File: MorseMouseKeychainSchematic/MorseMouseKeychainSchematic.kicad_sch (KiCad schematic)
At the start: 10 parts, among them J1 TP4056 with Protecive Diode, J2 ESP32-C3 SuperMini, J3 HW-504 Joystick Controller, J4 5v Boost Converter, J5 USB_C_Receptacle_USB2.0_16P, SW1 SW_Push

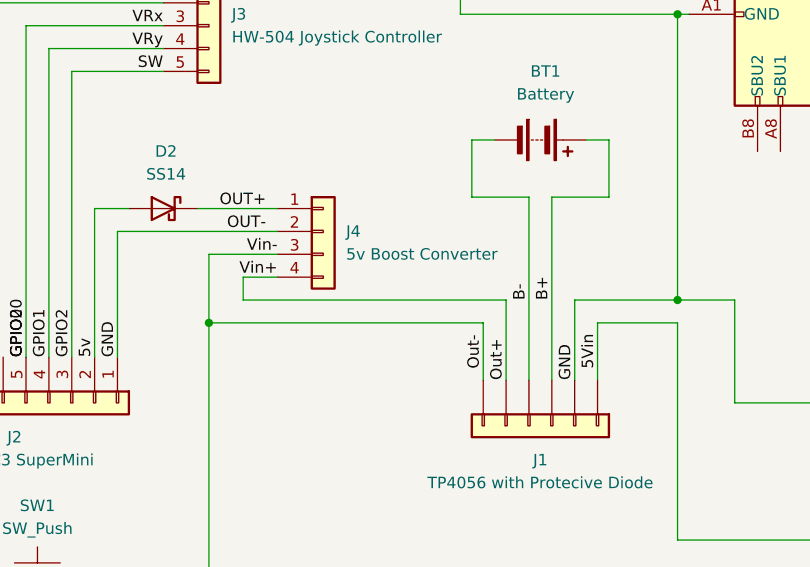
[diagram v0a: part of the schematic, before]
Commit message: Migrate to ESP32-S3 USB HID architecture and power optimization
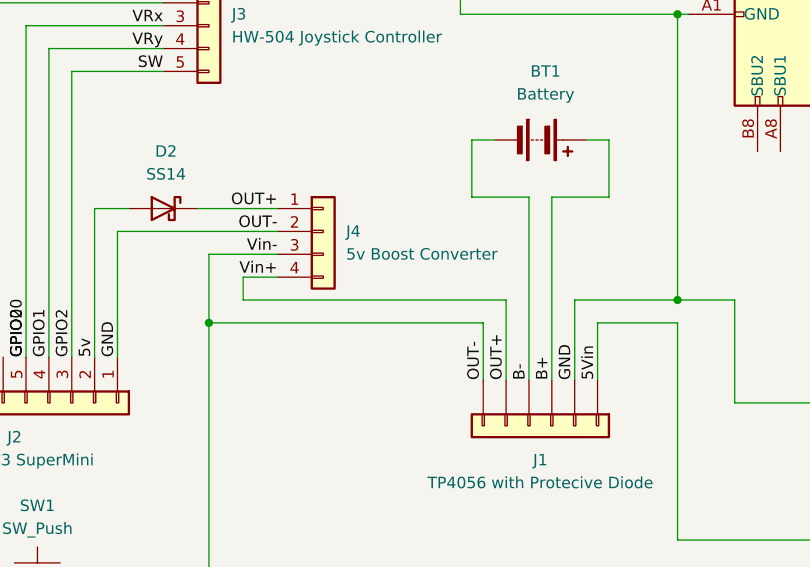
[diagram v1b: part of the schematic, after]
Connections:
- net Out+ is gone; now on net OUT+: J1.5 (Pin_5), J4.4 (Pin_4)

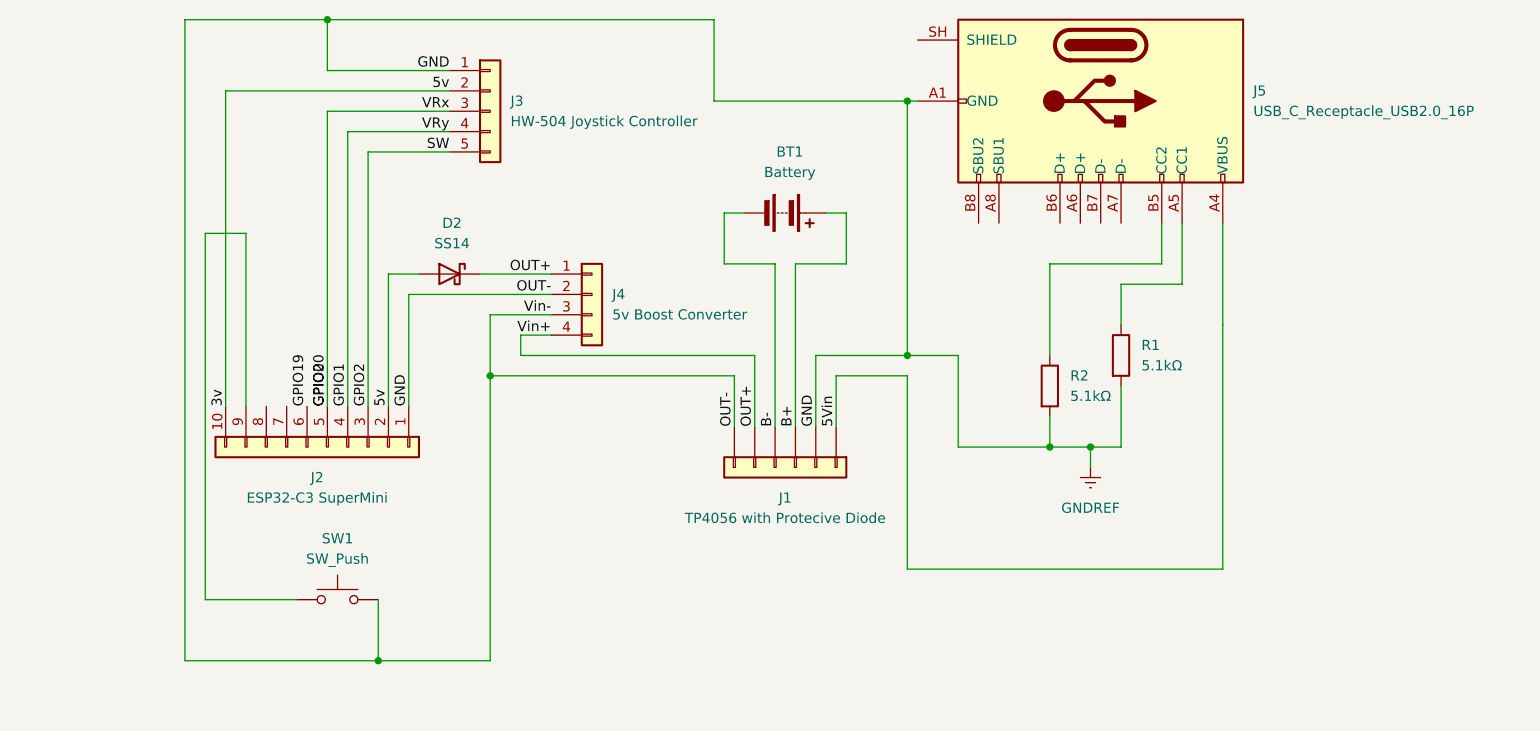
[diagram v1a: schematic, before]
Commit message: Complete firmware v1: USB HID, BLE HID, Morse commands, power optimization
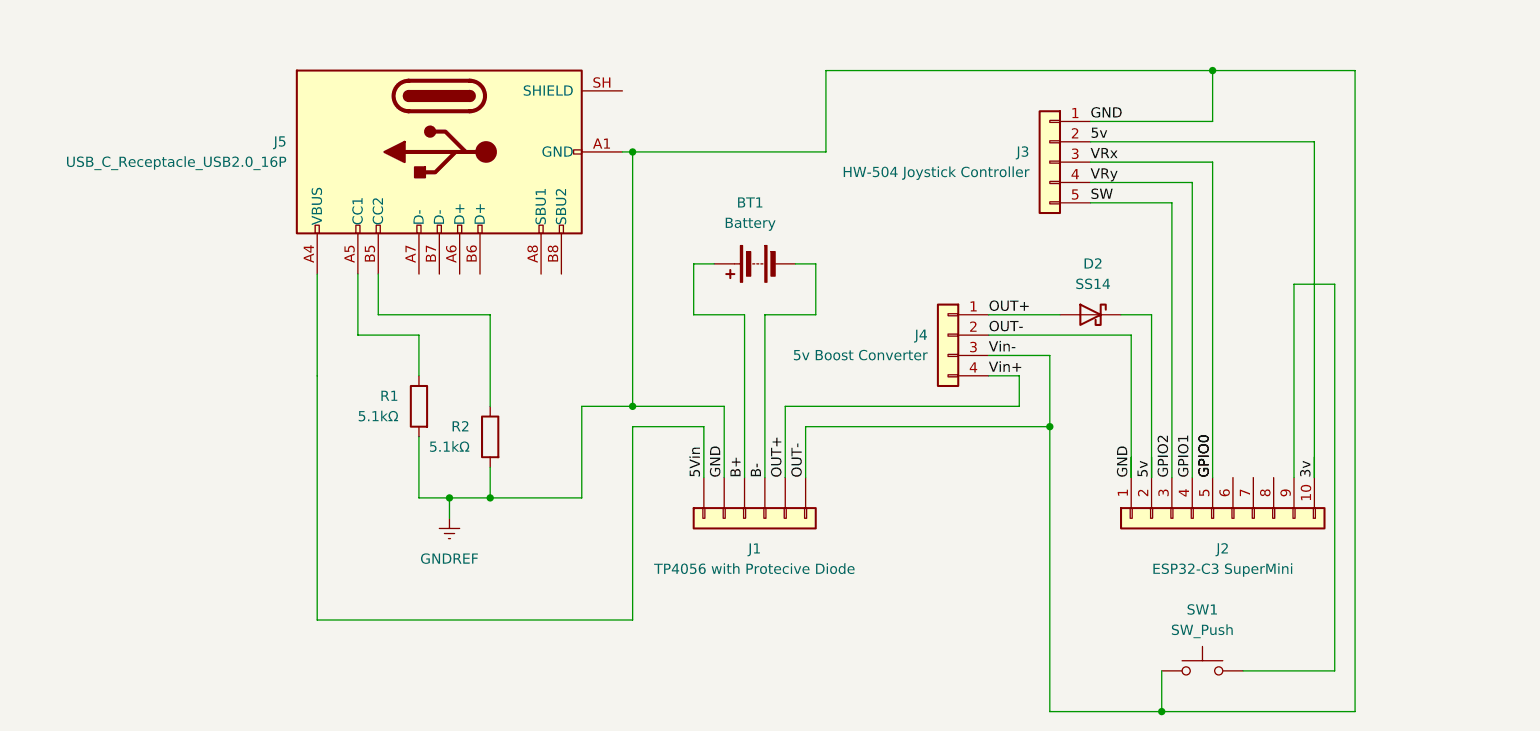
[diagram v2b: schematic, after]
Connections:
- net 3v: now also D2.1 (K); no longer D2.2 (A)
- net OUT+: now also D2.2 (A); no longer D2.1 (K)
- net GPIO19: no longer names the net of J2.6 (Pin_6)
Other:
- moved on the sheet: BT1, D2, J1, J2, J3, J4, J5, R1, R2, SW1

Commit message: with switch
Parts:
- added SW2: SW_SPST, symbol Switch:SW_SPST
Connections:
- net OUT+: now also SW2.1 (A); no longer J4.4 (Pin_4)
- new net Vin+: J4.4 (Pin_4), SW2.2 (B)
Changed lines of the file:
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@@
+	)
+	(junction
+		(at 119.38 66.04)
+		(diameter 0)
+		(color 0 0 0 0)
 	)
 	(junction
@@
 	(wire
 		(pts
+			(xy 115.57 66.04) (xy 119.38 66.04)
+		)
+		(stroke
+			(width 0)
+			(type default)
+			(color 255 0 8 1)
+		)
+	)
+	(wire
+		(pts
 			(xy 64.77 54.61) (xy 78.74 54.61)
 		)
@@
 	(wire
 		(pts
+			(xy 129.54 66.04) (xy 144.78 66.04)
+		)
+		(stroke
+			(width 0)
+			(type default)
+			(color 255 0 8 1)
+		)
+	)
+	(wire
+		(pts
 			(xy 181.61 33.02) (xy 181.61 74.93)
 		)
@@
 	(wire
 		(pts
-			(xy 115.57 66.04) (xy 144.78 66.04)
+			(xy 119.38 66.04) (xy 120.65 66.04)
 		)
 		(stroke
@@
 	)
 	(symbol
+		(lib_id "Switch:SW_SPST")
+		(at 124.46 66.04 0)
+		(unit 1)
+		(body_style 1)
+		(exclude_from_sim no)
+		(in_bom yes)
+		(on_board yes)
+		(in_pos_files yes)
+		(dnp no)
+		(fields_autoplaced yes)
+		(property "Reference" "SW2"
+			(at 124.46 59.69 0)
+			(show_name no)
+			(do_not_autoplace no)
+			(effects
+				(font
+					(size 1.27 1.27)
+				)
+			)
+		)
+		(property "Value" "SW_SPST"
+			(at 124.46 62.23 0)
+			(show_name no)
+			(do_not_autoplace no)
+			(effects
+				(font
+					(size 1.27 1.27)
+				)
+			)
+		)
+		(property "Footprint" ""
+			(at 124.46 66.04 0)
+			(hide yes)
+			(show_name no)
+			(do_not_autoplace no)
+			(effects
+				(font
+					(size 1.27 1.27)
+				)
+			)
+		)
+		(property "Datasheet" ""
+			(at 124.46 66.04 0)
+			(hide yes)
+			(show_name no)
+			(do_not_autoplace no)
+			(effects
+				(font
+					(size 1.27 1.27)
+				)
+			)
+		)
+		(property "Description" "Single Pole Single Throw (SPST) switch"
+			(at 124.46 66.04 0)
+			(hide yes)
+			(show_name no)
+			(do_not_autoplace no)
+			(effects
+				(font
+					(size 1.27 1.27)
+				)
+			)
+		)
+		(pin "1"
+		)
+		(pin "2"
+		)
+		(instances
+			(project "MorseMouseKeychainSchematic"
+				(path "/36179d4a-9247-48db-9ba3-a22c64180de0"
+					(reference "SW2")
+					(unit 1)
+				)
+			)
+		)
+	)
+	(symbol
 		(lib_id "Device:R")
 		(at 69.85 66.04 0)
@@
 		(in_pos_files yes)
 		(dnp no)
-		(fields_autoplaced yes)
 		(property "Reference" "J4"
 			(at 133.35 57.1499 0)
@@
 		)
 		(property "Value" "5v Boost Converter"
-			(at 133.35 59.6899 0)
-			(show_name no)
-			(do_not_autoplace no)
+			(at 144.526 50.038 0)
+			(show_name no)
+			(do_not_autoplace no)
